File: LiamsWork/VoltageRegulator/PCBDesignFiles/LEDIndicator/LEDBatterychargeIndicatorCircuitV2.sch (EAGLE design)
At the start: 34 parts, among them U1 LM339AMSMD

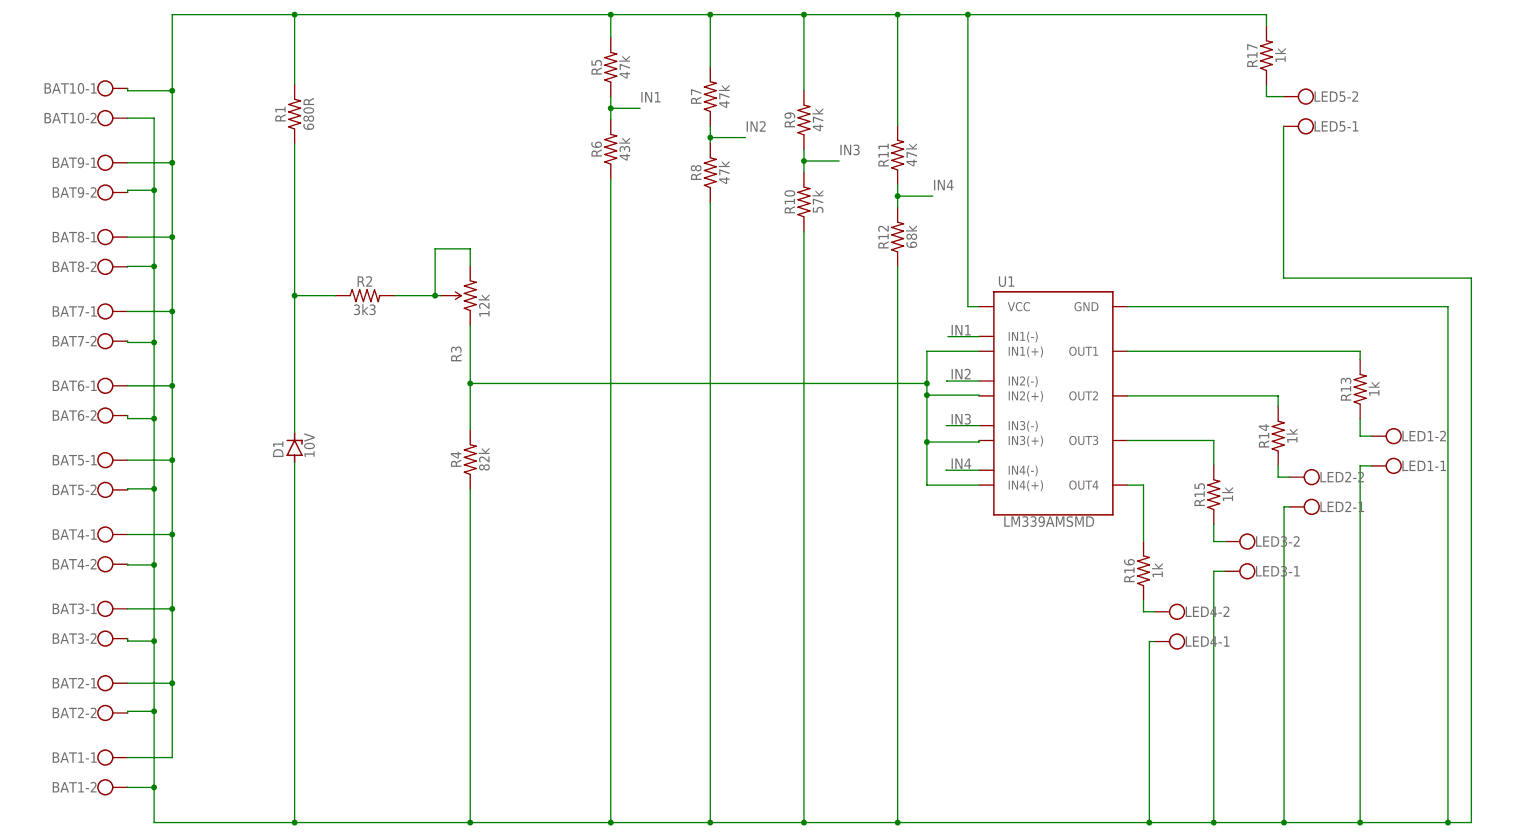
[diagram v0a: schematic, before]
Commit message: Files updated to contain recent developments, added Amplifier power supply file
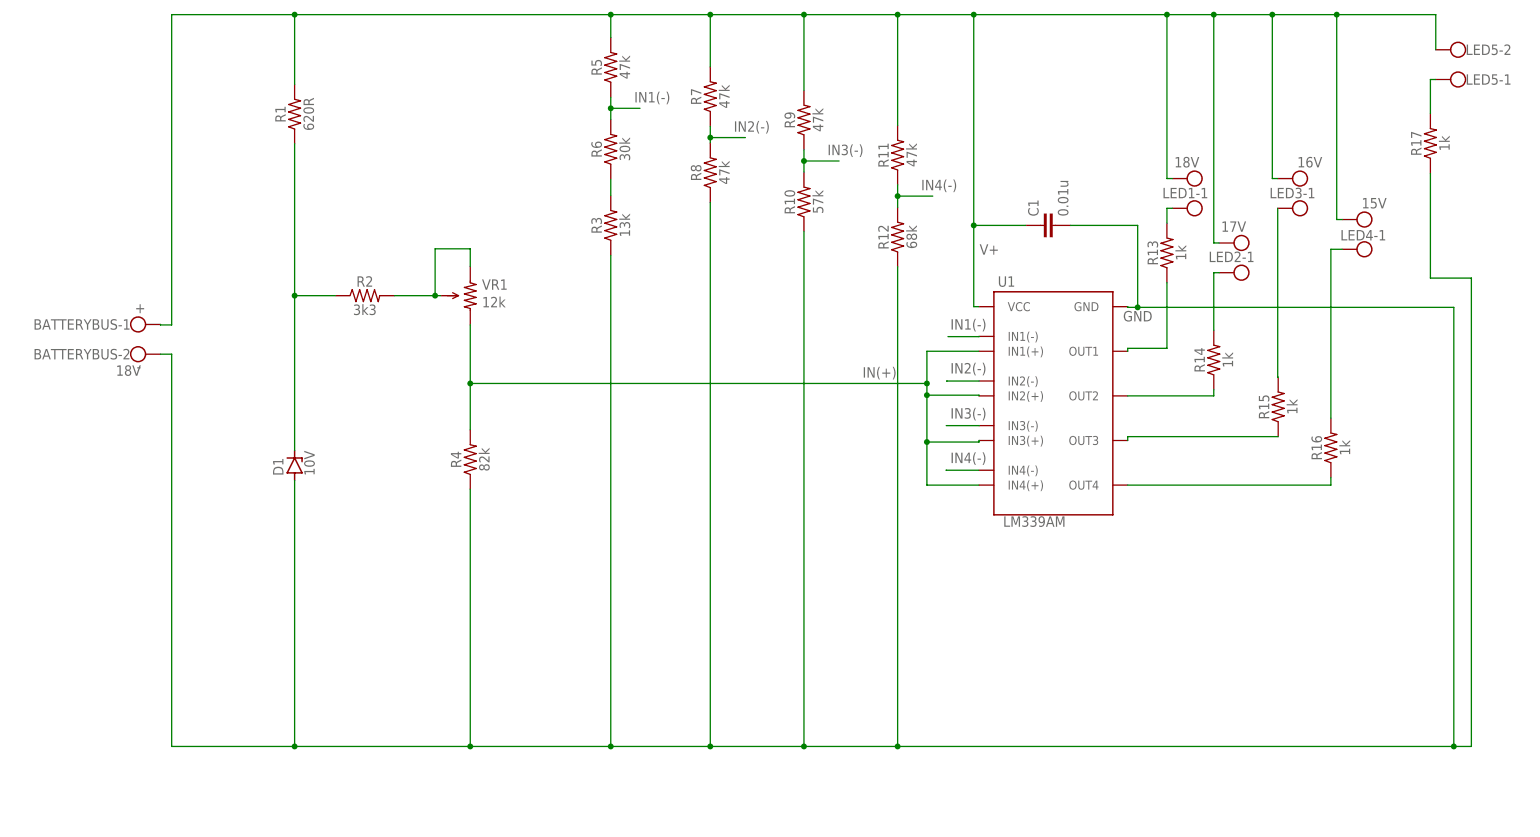
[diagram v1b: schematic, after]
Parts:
- removed BAT1, BAT10, BAT2, BAT3, BAT4, BAT5, BAT6, BAT7, BAT8, BAT9: (no value), con-wago-500:W237-102
- added BATTERYBUS: 18V, con-wago-500:W237-102
- added C1: 0.01u, SparkFun-Capacitors:0.33UF/330NF-0805-50V-10%
- added VR1: 12k, RequiredComponents:TRIMPOT3266W
- D1: device diode:ZENER-DIODEF126-12 -> diode:ZENER-DIODESOT23
- LED1: value (none) -> 18V
- LED2: value (none) -> 17V
- LED3: value (none) -> 16V
- LED4: value (none) -> 15V
- R1: value 680R -> 620R
- R3: value 12k -> 13k; device SparkFun-Retired:TRIMPOTPTH -> SparkFun-Resistors:RESISTOR0805
- R6: value 43k -> 30k
- U1: value LM339AMSMD -> LM339AM
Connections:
- net IN1 renamed IN1(-)
- net IN2 renamed IN2(-)
- net IN3 renamed IN3(-)
- net IN4 renamed IN4(-)
- removed net N$13: LED3-2.KL, R15.1
- removed net N$14: R16.2, U1.OUT4
- removed net N$15: LED4-2.KL, R16.1
- removed net N$16: LED5-2.KL, R17.1
- new net GND: BATTERYBUS-2.KL, C1.2, D1.A, R10.1, R12.1, R17.1, R3.1, R4.1, R8.1, U1.GND
- new net IN(+): R4.2, U1.IN1(+), U1.IN2(+), U1.IN3(+), U1.IN4(+), VR1.1
- new net N$1: LED5-1.KL, R17.2
- new net N$3: R13.1, U1.OUT1
- new net V+: BATTERYBUS-1.KL, C1.1, LED1-2.KL, LED2-2.KL, LED3-2.KL, LED4-2.KL, LED5-2.KL, R1.2, R11.2, R5.2, R7.2, R9.2, U1.VCC
- net N$10: now also R16.1, U1.OUT4; no longer LED2-2.KL, R14.1
- net N$11: now also LED4-1.KL, R16.2; no longer R15.2, U1.OUT3
- net N$12: now also R3.2, R6.1; no longer R3.CCW, R4.2, U1.IN1(+), U1.IN2(+), U1.IN3(+), U1.IN4(+)
- net N$2: now also LED1-1.KL, R13.2; no longer BAT1-1.KL, BAT10-1.KL, BAT2-1.KL, BAT3-1.KL, BAT4-1.KL, BAT5-1.KL, BAT6-1.KL, BAT7-1.KL, BAT8-1.KL, BAT9-1.KL, R1.2, R11.2, R17.2, R5.2, R7.2, R9.2, U1.VCC
- net N$5: now also R14.1, U1.OUT2; no longer R13.2, U1.OUT1
- net N$6: now also VR1.3, VR1.WIPER; no longer R3.CW, R3.WIPER
- net N$7: now also R14.2; no longer BAT1-2.KL, BAT10-2.KL, BAT2-2.KL, BAT3-2.KL, BAT4-2.KL, BAT5-2.KL, BAT6-2.KL, BAT7-2.KL, BAT8-2.KL, BAT9-2.KL, D1.A, LED1-1.KL, LED3-1.KL, LED4-1.KL, LED5-1.KL, R10.1, R12.1, R4.1, R6.1, R8.1, U1.GND
- net N$8: now also LED3-1.KL, R15.2; no longer LED1-2.KL, R13.1
- net N$9: now also R15.1, U1.OUT3; no longer R14.2, U1.OUT2
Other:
- note added: "+"
- note added: "-"
- moved on the sheet: D1, LED1-1, LED2-1, LED3-1, LED4-1, LED5-1, LED5-2, R13, R14, R15, R16, R17
